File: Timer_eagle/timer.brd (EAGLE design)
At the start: 100 x 50 mm, 21 parts, among them IC1 NE555, IC2 4081N, IC3 4518N, IC4 4070N, K1 G5L, Q1 BC548, Q2 TIP120, X1 SSW-103-02-S-S

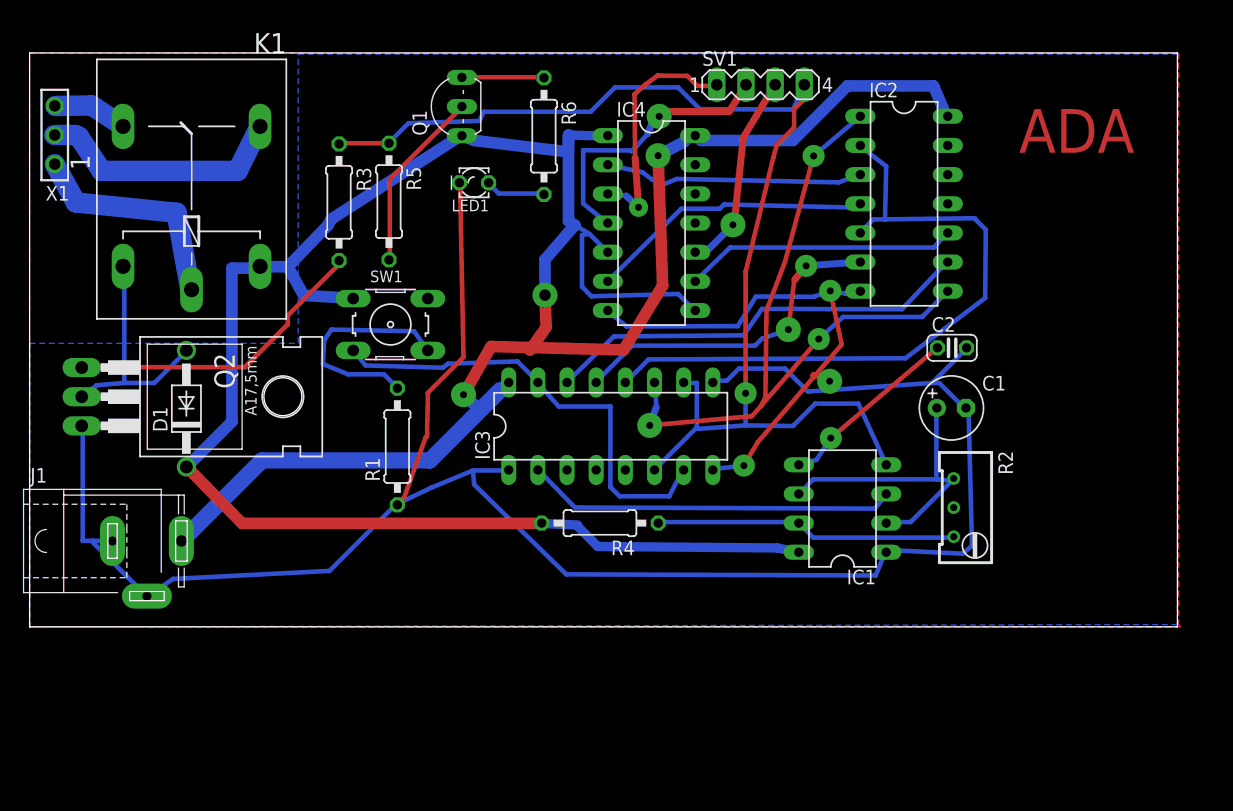
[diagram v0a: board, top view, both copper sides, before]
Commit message: Esquemático Corrigido (Ligação RES_555) Projeto da Placa refeito
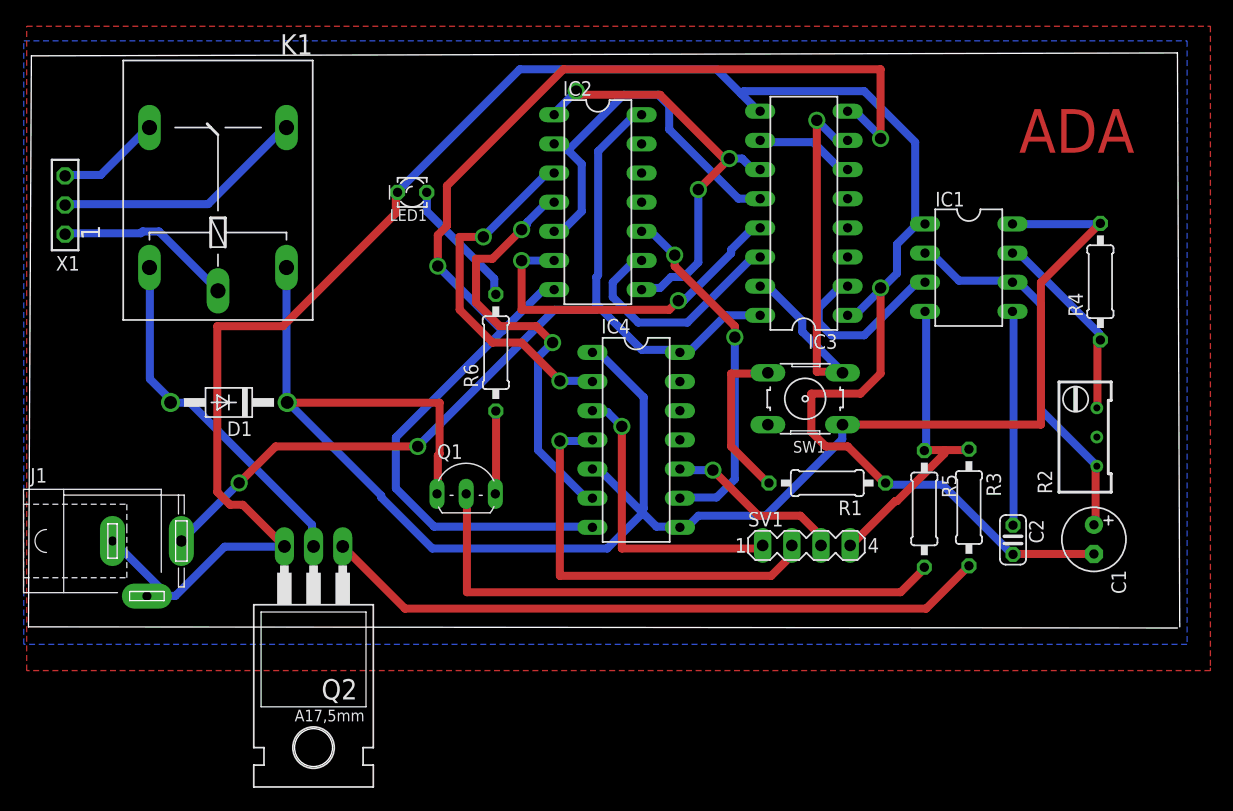
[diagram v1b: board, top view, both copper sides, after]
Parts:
- moved R3 61.0 mm to (81.8, 10.4)
- moved R5 53.8 mm to (77.9, 10.3)
- moved R4 48.4 mm to (93.3, 30.1), turned to 90 degrees
- moved SV1 40.3 mm to (67.7, 7.09)
- moved R1 37.6 mm to (69.5, 12.5), turned to 180 degrees
- moved SW1 36.7 mm to (67.6, 19.9), turned to 180 degrees
- moved Q1 32.5 mm to (38.0, 12.9), turned to 0 degrees
- moved IC2 26.7 mm to (49.5, 37.0)
- moved IC3 25.0 mm to (67.5, 36.0), turned to 90 degrees
- moved Q2 23.8 mm to (24.7, 0.66), turned to 180 degrees
- moved IC1 23.7 mm to (81.8, 31.3), turned to 270 degrees
- moved R6 19.3 mm to (40.6, 23.9), turned to 90 degrees
- moved IC4 18.9 mm to (52.8, 16.3)
- moved C2 17.5 mm to (85.7, 7.58), turned to 270 degrees
- moved C1 16.9 mm to (92.7, 7.62), turned to 270 degrees
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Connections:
- new net Q3_EN2: IC3.10, IC3.6
- net RESET_555: no longer IC3.10, IC3.6
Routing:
- net RESET_555: track 106.9 -> 28.1 mm, vias 1 -> 0
- net VSS: track 45.3 -> 109.4 mm
- net N$22: track 16.0 -> 49.4 mm
- net N$3: track 26.9 -> 58.3 mm
- net N$9: track 59.3 -> 34.1 mm
- net N$8: track 62.4 -> 37.9 mm
- net VDD: track 98.1 -> 80.7 mm
- net N$11: track 37.8 -> 20.7 mm
- net N$2: track 32.4 -> 16.2 mm
- net N$18: track 24.9 -> 37.2 mm, vias 0 -> 2
- net N$15: track 24.6 -> 36.4 mm
- net GND: track 174.7 -> 186.2 mm, vias 0 -> 1
- net N$16: track 20.9 -> 31.2 mm
- net N$4: track 26.4 -> 17.2 mm
- net Q3_EN2: track 0.00 -> 8.74 mm
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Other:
- board size 100 x 50 mm -> 100.3 x 50.1 mm

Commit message: As trilhas foram engrossadas, o VCC foi ligado com o VDD, o VSS foi ligado com o GND
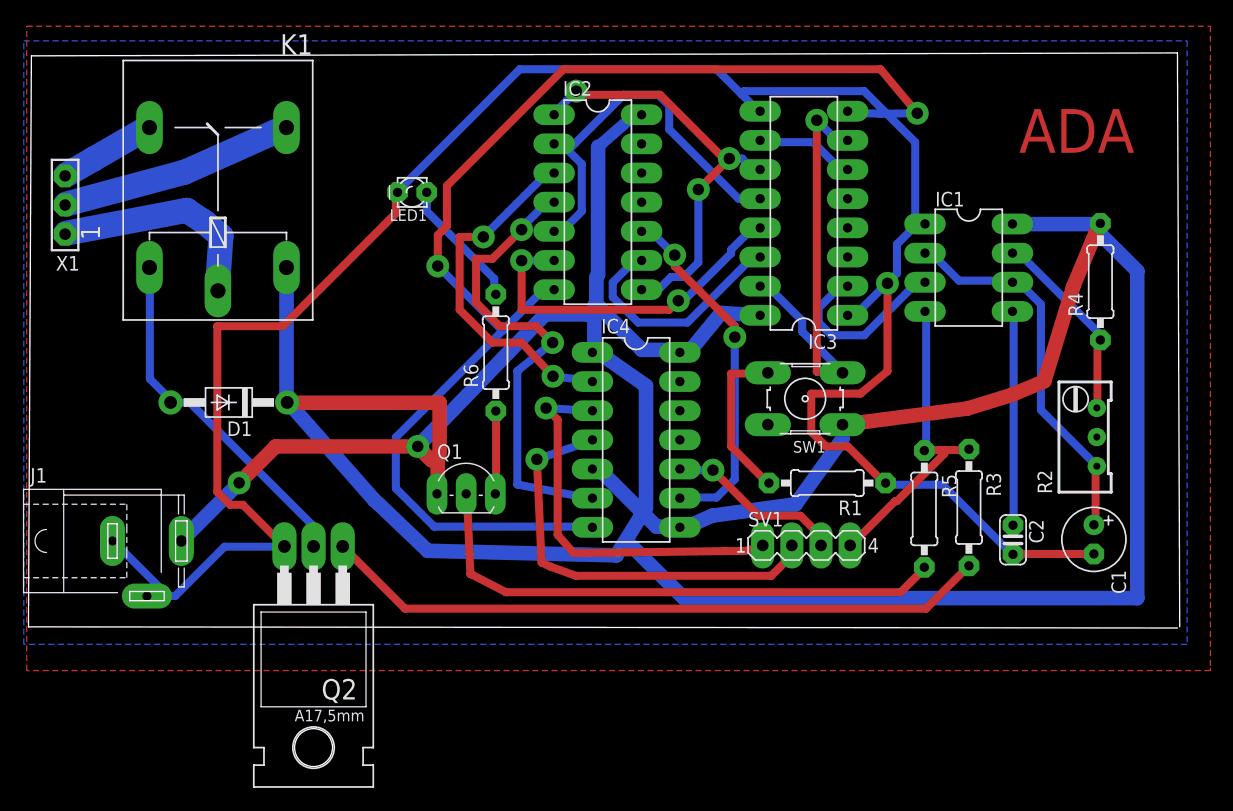
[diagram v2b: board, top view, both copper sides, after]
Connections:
- removed net GND: C1.-, C2.2, IC1.1, IC3.1, IC3.9, J1.1, J1.2, LED1.K, Q2.E, R1.1
- removed net VCC: D1.C, IC1.8, IC4.1, IC4.5, IC4.8, K1.1, Q1.C, R4.2, SW1.1
- net VDD: now also D1.C, IC1.8, IC4.1, IC4.5, IC4.8, K1.1, Q1.C, R4.2, SW1.1
- net VSS: now also C1.-, C2.2, IC1.1, IC3.1, IC3.9, J1.1, J1.2, LED1.K, Q2.E, R1.1
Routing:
- net VDD: track 80.7 -> 321.9 mm
- net VSS: track 109.4 -> 297.7 mm, vias 2 -> 3
- net GND: track 186.2 -> 0.00 mm, vias 1 -> 0
- net VCC: track 159.9 -> 0.00 mm
- net N$12: track 26.2 -> 36.9 mm
- net N$25: track 0.00 -> 4.40 mm
- net N$18: track 37.2 -> 41.4 mm
- net N$19: track 15.6 -> 19.4 mm
- net N$20: track 22.1 -> 20.5 mm
- net N$22: track 49.4 -> 47.9 mm
- net N$15: track 36.4 -> 37.7 mm
- net N$21: track 9.09 -> 8.49 mm
- added copper zone on layer 1, net VSS
- added copper zone on layer 16, net VSS
- removed copper zone on layer 1, net GND
- removed copper zone on layer 16, net GND

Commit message: Projeto final da placa
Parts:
- removed X1: SSW-103-02-S-S, con-samtec:SSW-103-02-S-S
- added JP1, JP2, JP3: (no value), pinhead:1X01
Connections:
- net N$19: now also JP1.1; no longer X1.1
- net N$20: now also JP2.1; no longer X1.2
- net N$21: now also JP3.1; no longer X1.3
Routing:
- net VSS: track 297.7 -> 332.2 mm
- net N$9: track 34.1 -> 36.0 mm
- net N$10: track 31.0 -> 32.7 mm
- net N$17: track 30.9 -> 32.5 mm
- net N$8: track 37.9 -> 39.2 mm
- net N$2: track 16.2 -> 17.5 mm
- net VDD: track 321.9 -> 323.1 mm
- net N$16: track 31.2 -> 32.3 mm
- net N$20: track 20.5 -> 21.6 mm
- net N$6: track 38.6 -> 39.6 mm
- net N$11: track 20.7 -> 21.7 mm
- net N$15: track 37.7 -> 38.7 mm
- net N$21: track 8.49 -> 7.65 mm
- net N$18: track 41.4 -> 42.0 mm
- net N$4: track 17.2 -> 17.8 mm
